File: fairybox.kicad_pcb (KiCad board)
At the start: 2 copper layers, 91.4 x 55.9 mm, 67 parts, among them J1 REED, Q1 locked, Q10 locked, Q2 locked, Q3 locked, Q4 locked, Q5 locked, Q6 locked, Q7 locked, Q8 locked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

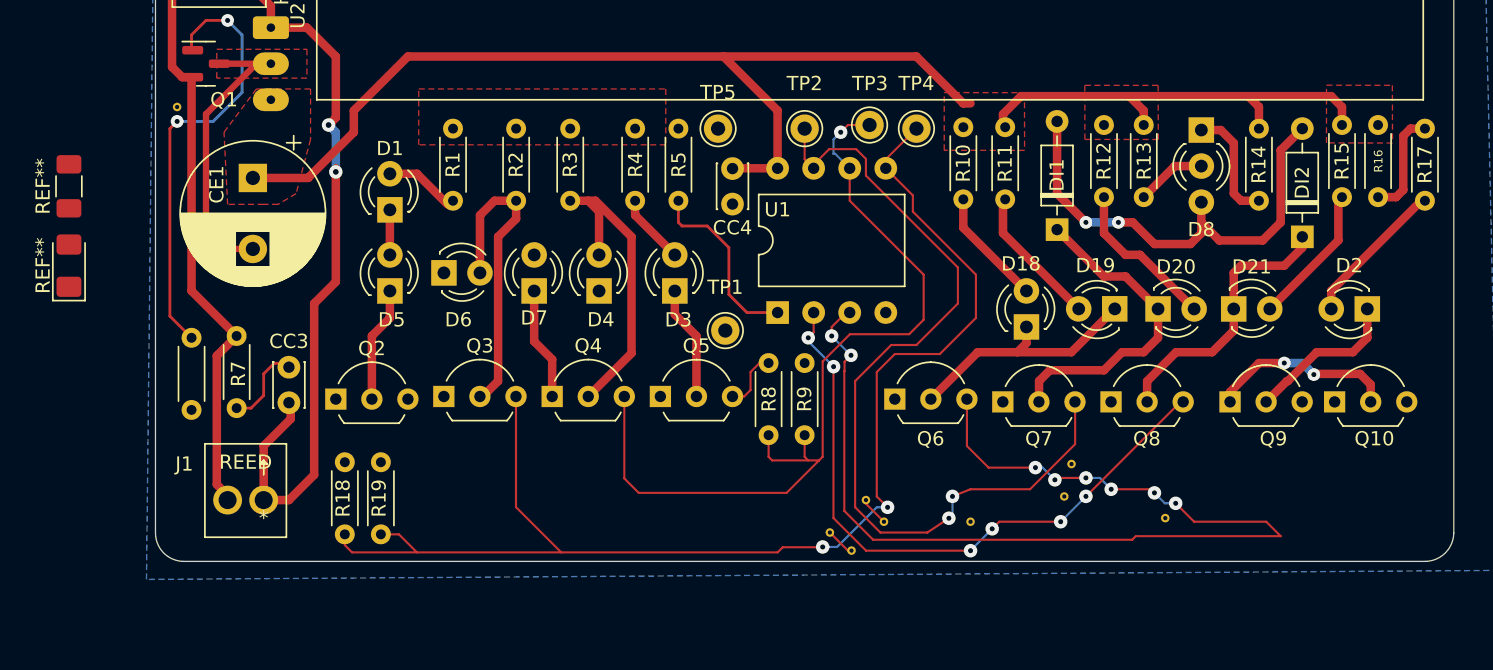
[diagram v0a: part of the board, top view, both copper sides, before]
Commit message: GPIO Assignment Changes
In order to enable more efficient signal trace routing transistor base pins were reassigned to different MCU signal pins. The new order no longer has signal traces crossing paths to get to their destination. In other words, it's eliminated the need for any vias to the ground plane. 

This routing is much simpler and improves the chances of a successful (functioning) PCB. 
- Easier to manufacture. Not pushing JLCPCB's manufacturing capabilities is a good thing.
- Likely less unintended EMI radiation. 
- Less opportunities for signal crosstalk.
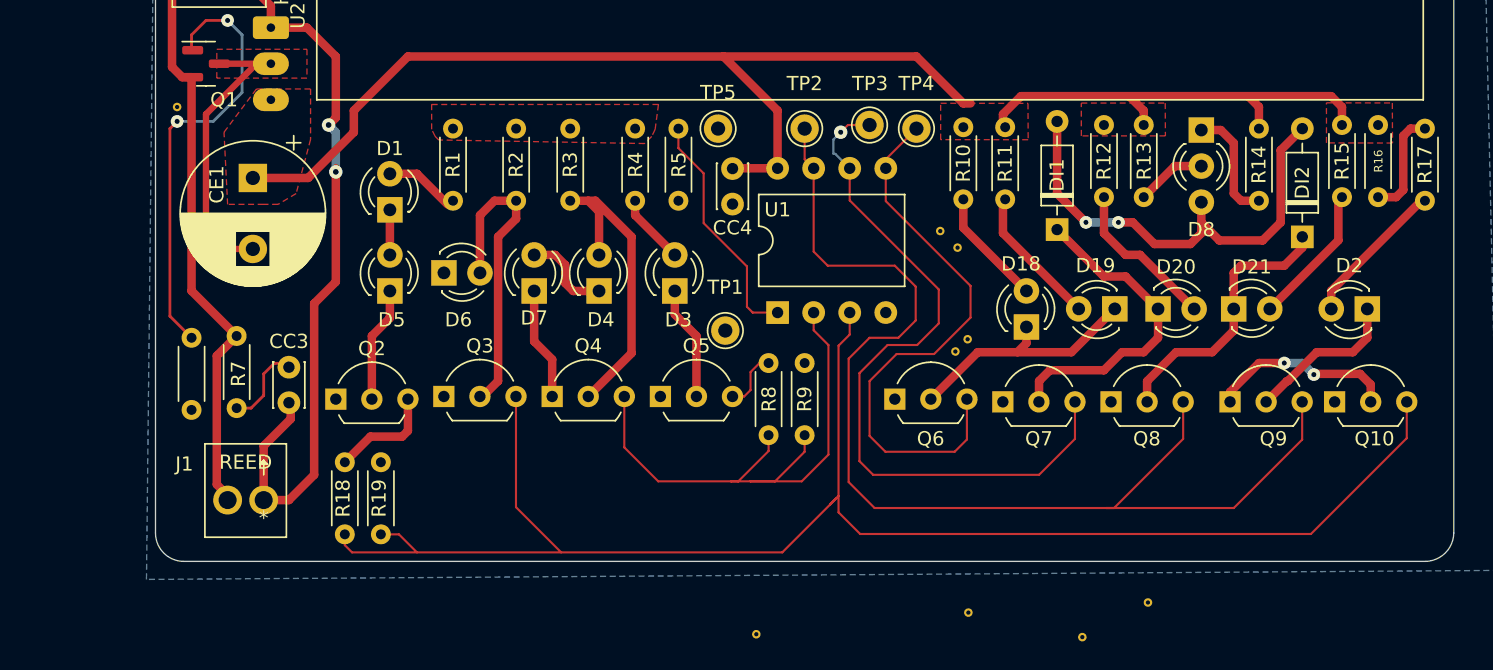
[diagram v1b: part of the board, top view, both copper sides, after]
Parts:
- removed REF**: LED_1206_3216Metric_Pad1.42x1.75mm_HandSolder, LED_SMD:LED_1206_3216Metric_Pad1.42x1.75mm_HandSolder
- removed REF**: R_1206_3216Metric_Pad1.30x1.75mm_HandSolder, Resistor_SMD:R_1206_3216Metric_Pad1.30x1.75mm_HandSolder
- moved JP2 23.8 mm to (93.1, 111.8)
- moved JP7 20.0 mm to (107.3, 84.6)
- moved JP3 19.7 mm to (106.1, 83.4)
- moved JP9 17.0 mm to (108.0, 91.0)
- moved JP6 15.5 mm to (107.1, 91.9)
- moved JP5 12.2 mm to (116.1, 112.0)
- moved JP8 6.40 mm to (108.1, 110.3)
- moved JP4 6.07 mm to (120.7, 109.6)
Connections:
- Q3 pad 3: /MCU GPIO0 MOSI -> /MCU GPIO4
- Q4 pad 3: /MCU GPIO1 MISO -> /MCU GPIO3
- Q6 pad 3: /MCU GPIO4 -> /MCU GPIO0 MOSI
- Q7 pad 3: /MCU GPIO2 SCK -> /MCU GPIO1 MISO
- Q8 pad 3: /MCU GPIO3 -> /MCU GPIO2 SCK
- Q9 pad 3: /MCU GPIO0 MOSI -> /MCU GPIO2 SCK
- R18 pad 1: /MCU GPIO0 MOSI -> /MCU GPIO4
- R19 pad 1: /MCU GPIO0 MOSI -> /MCU GPIO4
- R5 pad 1: +5V -> Net-(R5-Pad1)
- R5 pad 2: Net-(U1-Pad1) -> +5V
- R8 pad 1: /MCU GPIO1 MISO -> /MCU GPIO3
- R9 pad 1: /MCU GPIO1 MISO -> /MCU GPIO3
- TP1 pad 1: /MCU RST -> +5V
- U1 pad 1: Net-(U1-Pad1) -> Net-(R5-Pad1)
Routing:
- net /MCU GPIO0 MOSI: track 90.5 -> 39.4 mm, vias 2 -> 0
- net /MCU GPIO4: track 75.3 -> 113.8 mm, vias 8 -> 0
- net /MCU GPIO2 SCK: track 61.2 -> 81.5 mm, vias 2 -> 0
- net Net-(R5-Pad1): track 0.00 -> 16.9 mm
- net Net-(U1-Pad1): track 13.1 -> 0.00 mm
- net /MCU GPIO1 MISO: track 61.9 -> 51.5 mm
- net /Q2_BASE: track 0.00 -> 7.60 mm
- net /D7_AN: track 0.00 -> 6.37 mm
- net /MCU GPIO3: track 45.6 -> 40.7 mm, vias 6 -> 0
- net GND: track 33.4 -> 29.3 mm

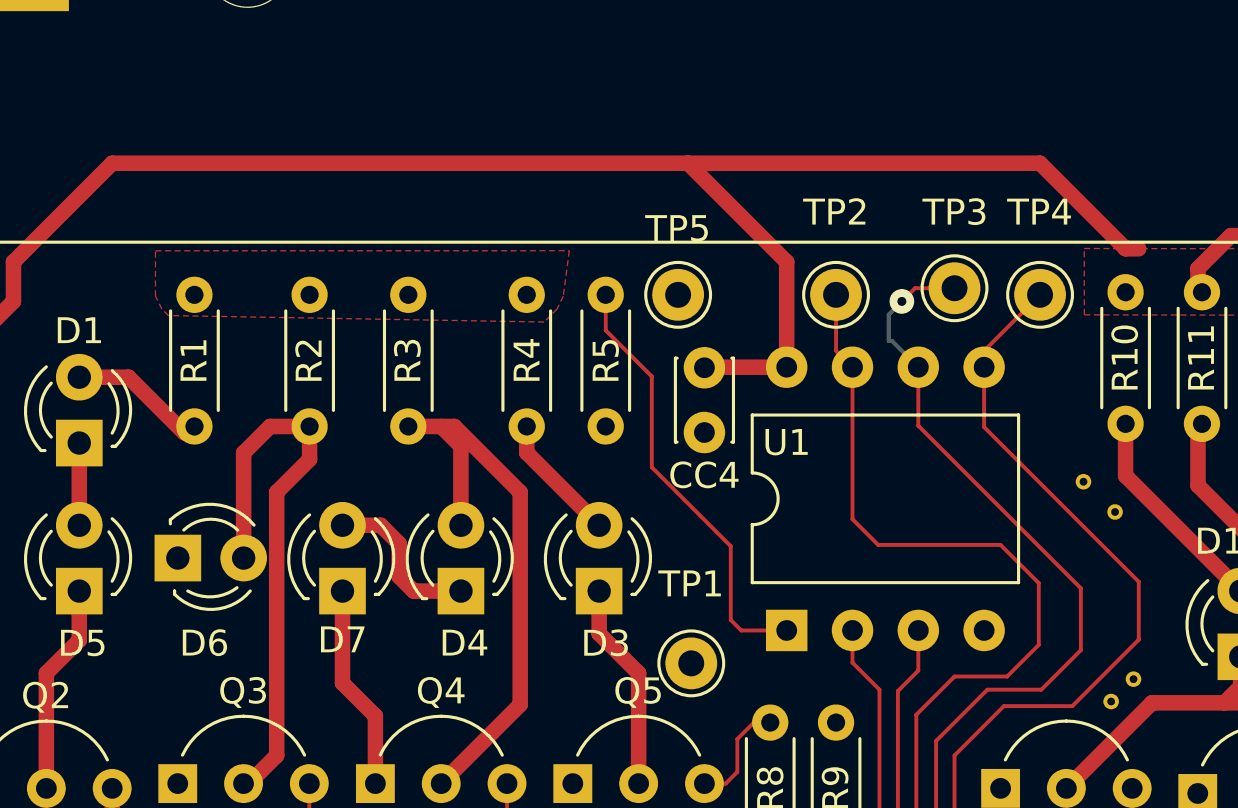
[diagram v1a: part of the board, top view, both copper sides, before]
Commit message: MCU reset pin and resistor fix
Attiny85 Reset Pin 
- Rotated pull-up resistor R5. 5V pad now faces north.
- Extended 5V copper pour to include R5
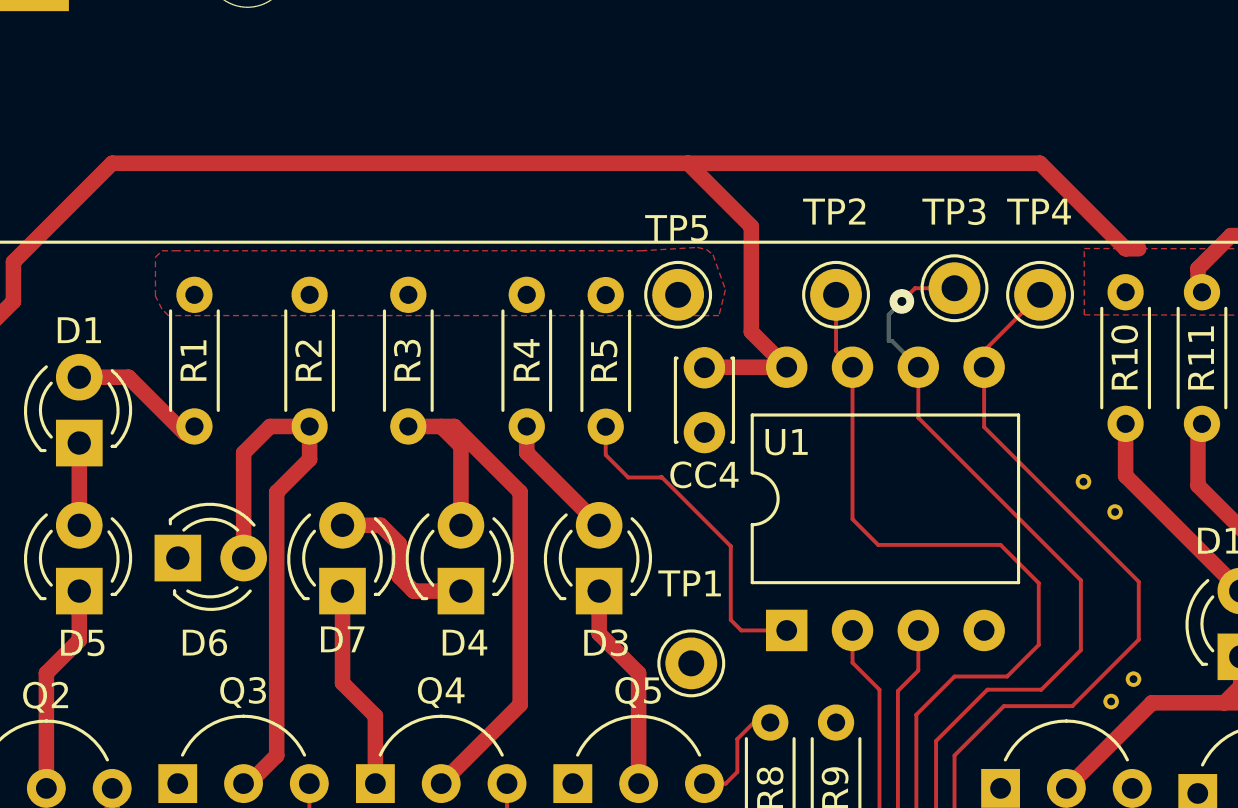
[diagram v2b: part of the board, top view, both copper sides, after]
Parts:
- moved R5 5.09 mm to (87.6, 81.3), turned to 90 degrees
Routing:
- net Net-(R5-Pad1): track 16.9 -> 12.6 mm
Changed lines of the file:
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@@
   )
   (footprint "Resistor_THT:R_Axial_DIN0204_L3.6mm_D1.6mm_P5.08mm_Horizontal" (layer "F.Cu")
-    (at 87.63 76.2 -90)
+    (at 87.63 81.29 90)
     (descr "Resistor, Axial_DIN0204 series, Axial, Horizontal, pin pitch=5.08mm, 0.167W, length*diameter=3.6*1.6mm^2, http://cdn-reichelt.de/documents/datenblatt/B400/1_4W%23YAG.pdf")
     (tags "Resistor Axial_DIN0204 series Axial Horizontal pin pitch 5.08mm 0.167W length 3.6mm diameter 1.6mm")
@@
       (effects (font (size 1 1) (thickness 0.15)))
     )
-    (fp_text value locked "10K" (at 2.54 -0.254 -90) (layer "F.Fab")
-      (effects (font (size 0.8 0.8) (thickness 0.15)))
-    )
-    (fp_text user locked "${REFERENCE}" (at -1.524 0 180) (layer "F.Fab")
+    (fp_text value locked "10K" (at 2.54 -0.254 90) (layer "F.Fab")
+      (effects (font (size 0.8 0.8) (thickness 0.15)))
+    )
+    (fp_text user locked "${REFERENCE}" (at -1.524 0) (layer "F.Fab")
       (effects (font (size 0.72 0.72) (thickness 0.108)))
     )
@@
     (fp_line (start 5.08 0) (end 4.34 0) (layer "F.Fab") (width 0.1))
     (fp_line (start 4.34 -0.8) (end 0.74 -0.8) (layer "F.Fab") (width 0.1))
-    (pad "1" thru_hole circle (at 0 0 270) (size 1.4 1.4) (drill 0.7) (layers *.Cu *.Mask)
+    (pad "1" thru_hole circle (at 0 0 90) (size 1.4 1.4) (drill 0.7) (layers *.Cu *.Mask)
       (net 8 "Net-(R5-Pad1)") (pintype "passive"))
-    (pad "2" thru_hole oval (at 5.08 0 270) (size 1.4 1.4) (drill 0.7) (layers *.Cu *.Mask)
+    (pad "2" thru_hole oval (at 5.08 0 90) (size 1.4 1.4) (drill 0.7) (layers *.Cu *.Mask)
       (net 13 "+5V") (pintype "passive"))
     (model "${KICAD6_3DMODEL_DIR}/Resistor_THT.3dshapes/R_Axial_DIN0204_L3.6mm_D1.6mm_P5.08mm_Horizontal.wrl"
@@
   (segment (start 108.204 87.2744) (end 102.235 81.3054) (width 0.15) (layer "F.Cu") (net 7))
   (segment (start 102.997 92.075) (end 105.6386 92.075) (width 0.15) (layer "F.Cu") (net 7))
-  (segment (start 87.63 76.2) (end 87.63 77.5716) (width 0.15) (layer "F.Cu") (net 8))
-  (segment (start 89.408 82.8548) (end 92.456 85.9028) (width 0.15) (layer "F.Cu") (net 8))
+  (segment (start 89.7766 83.2234) (end 89.75 83.25) (width 0.15) (layer "F.Cu") (net 8))
   (segment (start 92.456 85.9028) (end 92.456 88.7476) (width 0.15) (layer "F.Cu") (net 8))
+  (segment (start 87.63 82.38) (end 87.63 81.29) (width 0.15) (layer "F.Cu") (net 8))
+  (segment (start 89.75 83.25) (end 88.5 83.25) (width 0.15) (layer "F.Cu") (net 8))
   (segment (start 92.456 88.7476) (end 92.8624 89.154) (width 0.15) (layer "F.Cu") (net 8))
   (segment (start 92.8624 89.154) (end 94.615 89.154) (width 0.15) (layer "F.Cu") (net 8))
-  (segment (start 89.408 79.3496) (end 89.408 82.8548) (width 0.15) (layer "F.Cu") (net 8))
-  (segment (start 87.63 77.5716) (end 89.408 79.3496) (width 0.15) (layer "F.Cu") (net 8))
+  (segment (start 89.7766 83.2234) (end 92.456 85.9028) (width 0.15) (layer "F.Cu") (net 8))
+  (segment (start 88.5 83.25) (end 87.63 82.38) (width 0.15) (layer "F.Cu") (net 8))
   (segment (start 100.4316 104.7496) (end 132.1816 104.7496) (width 0.15) (layer "F.Cu") (net 9))
   (segment (start 69.215 106.045) (end 67.945 104.775) (width 0.15) (layer "F.Cu") (net 9))
@@
   (segment (start 58.42 94.996) (end 57.531 95.885) (width 0.2) (layer "F.Cu") (net 12))
   (segment (start 111.76 73.914) (end 110.49 75.184) (width 0.6) (layer "F.Cu") (net 13))
-  (segment (start 94.615 74.93) (end 94.615 78.994) (width 0.6) (layer "F.Cu") (net 13))
   (segment (start 61.549677 79.674323) (end 57.658 79.674323) (width 0.6) (layer "F.Cu") (net 13))
   (segment (start 128.516 74.668) (end 128.516 76.2) (width 0.6) (layer "F.Cu") (net 13))
@@
   (segment (start 64.77 74.93) (end 68.58 71.12) (width 0.6) (layer "F.Cu") (net 13))
   (segment (start 94.615 78.994) (end 91.46 78.994) (width 0.6) (layer "F.Cu") (net 13))
-  (segment (start 90.805 71.12) (end 94.615 74.93) (width 0.6) (layer "F.Cu") (net 13))
   (segment (start 104.394 71.12) (end 107.696 74.422) (width 0.6) (layer "F.Cu") (net 13))
   (segment (start 110.49 75.184) (end 110.49 75.946) (width 0.6) (layer "F.Cu") (net 13))
@@
   (segment (start 119.38 73.914) (end 120.404 74.938) (width 0.6) (layer "F.Cu") (net 13))
   (segment (start 127.762 73.914) (end 128.516 74.668) (width 0.6) (layer "F.Cu") (net 13))
+  (segment (start 93.25 77.629) (end 94.615 78.994) (width 0.6) (layer "F.Cu") (net 13))
   (segment (start 134.366 74.676) (end 134.366 75.946) (width 0.6) (layer "F.Cu") (net 13))
+  (segment (start 90.805 71.12) (end 93.25 73.565) (width 0.6) (layer "F.Cu") (net 13))
   (segment (start 64.77 76.454) (end 61.549677 79.674323) (width 0.6) (layer "F.Cu") (net 13))
   (segment (start 90.805 71.12) (end 104.394 71.12) (width 0.6) (layer "F.Cu") (net 13))
   (segment (start 68.58 71.12) (end 90.805 71.12) (width 0.6) (layer "F.Cu") (net 13))
+  (segment (start 93.25 73.565) (end 93.25 77.629) (width 0.6) (layer "F.Cu") (net 13))
   (segment (start 81.788 81.28) (end 84.328 83.82) (width 0.6) (layer "F.Cu") (net 14))
   (segment (start 84.328 92.017) (end 81.28 95.065) (width 0.6) (layer "F.Cu") (net 14))
@@
   (segment (start 53.34 87.63) (end 53.34 72.6565) (width 0.6) (layer "F.Cu") (net 34))
   (segment (start 52.68324 72.578) (end 51.96476 71.85952) (width 0.6) (layer "F.Cu") (net 34))
+  (segment (start 104.4448 91.44) (end 102.362 91.44) (width 0.15) (layer "F.Cu") (net 35))
+  (segment (start 101.346 100.584) (end 113.03 100.584) (width 0.15) (layer "F.Cu") (net 35))
+  (segment (start 99.695 78.994) (end 99.695 80.945) (width 0.15) (layer "F.Cu") (net 35))
+  (segment (start 105.9688 87.2188) (end 105.9688 89.916) (width 0.15) (layer "F.Cu") (net 35))
+  (segment (start 100.3808 99.6188) (end 101.346 100.584) (width 0.15) (layer "F.Cu") (net 35))
+  (segment (start 100.3808 93.4212) (end 100.3808 99.6188) (width 0.15) (layer "F.Cu") (net 35))
+  (segment (start 115.56 98.054) (end 115.56 95.446) (width 0.15) (layer "F.Cu") (net 35))
+  (segment (start 102.362 91.44) (end 100.3808 93.4212) (width 0.15) (layer "F.Cu") (net 35))
   (segment (start 105.9688 89.916) (end 104.4448 91.44) (width 0.15) (layer "F.Cu") (net 35))
-  (segment (start 100.3808 99.6188) (end 101.346 100.584) (width 0.15) (layer "F.Cu") (net 35))
-  (segment (start 101.346 100.584) (end 113.03 100.584) (width 0.15) (layer "F.Cu") (net 35))
-  (segment (start 99.695 81.2546) (end 105.9688 87.5284) (width 0.15) (layer "F.Cu") (net 35))
-  (segment (start 99.695 78.994) (end 99.695 81.2546) (width 0.15) (layer "F.Cu") (net 35))
-  (segment (start 102.362 91.44) (end 100.3808 93.4212) (width 0.15) (layer "F.Cu") (net 35))
-  (segment (start 100.3808 93.4212) (end 100.3808 99.6188) (width 0.15) (layer "F.Cu") (net 35))
-  (segment (start 105.9688 87.5284) (end 105.9688 89.916) (width 0.15) (layer "F.Cu") (net 35))
-  (segment (start 104.4448 91.44) (end 102.362 91.44) (width 0.15) (layer "F.Cu") (net 35))
+  (segment (start 99.695 80.945) (end 105.9688 87.2188) (width 0.15) (layer "F.Cu") (net 35))
   (segment (start 101.092 75.946) (end 99.568 75.946) (width 0.15) (layer "F.Cu") (net 35))
   (segment (start 113.03 100.584) (end 115.56 98.054) (width 0.15) (layer "F.Cu") (net 35))
   (segment (start 99.568 75.946) (end 99.06 76.454) (width 0.15) (layer "F.Cu") (net 35))
-  (segment (start 115.56 98.054) (end 115.56 95.446) (width 0.15) (layer "F.Cu") (net 35))
   (via (at 99.06 76.454) (size 0.95) (drill 0.35) (layers "F.Cu" "B.Cu") (net 35))
   (segment (start 98.679 77.978) (end 99.695 78.994) (width 0.15) (layer "B.Cu") (net 35))
@@
     (polygon
       (pts
-        (xy 85.99087 76.252372)
-        (xy 85.75 76.75)
-        (xy 85.25 77.25)
+        (xy 89 74.5)
+        (xy 91.1606 74.3712)
+        (xy 91.5162 74.4474)
+        (xy 91.7702 74.6506)
+        (xy 92.25 76)
+        (xy 92 77)
         (xy 70.75 77)
         (xy 70.5 76.75)
         (xy 70.25 76.25)
-        (xy 70.25 74.5)
+        (xy 70.25 74.75)
+        (xy 70.5 74.5)
+        (xy 71 74.499893)
         (xy 86.224813 74.497712)
       )
